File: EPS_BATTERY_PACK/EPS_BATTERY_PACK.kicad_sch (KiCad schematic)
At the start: 47 parts, among them J6001 PT_1000, J6002 HEATER, J6003 HEATER, J6004 Battery, Q6001 NVTFWS4D9N04XMTAG, Q6002 NVTFWS4D9N04XMTAG, U6001 BQ76920PW

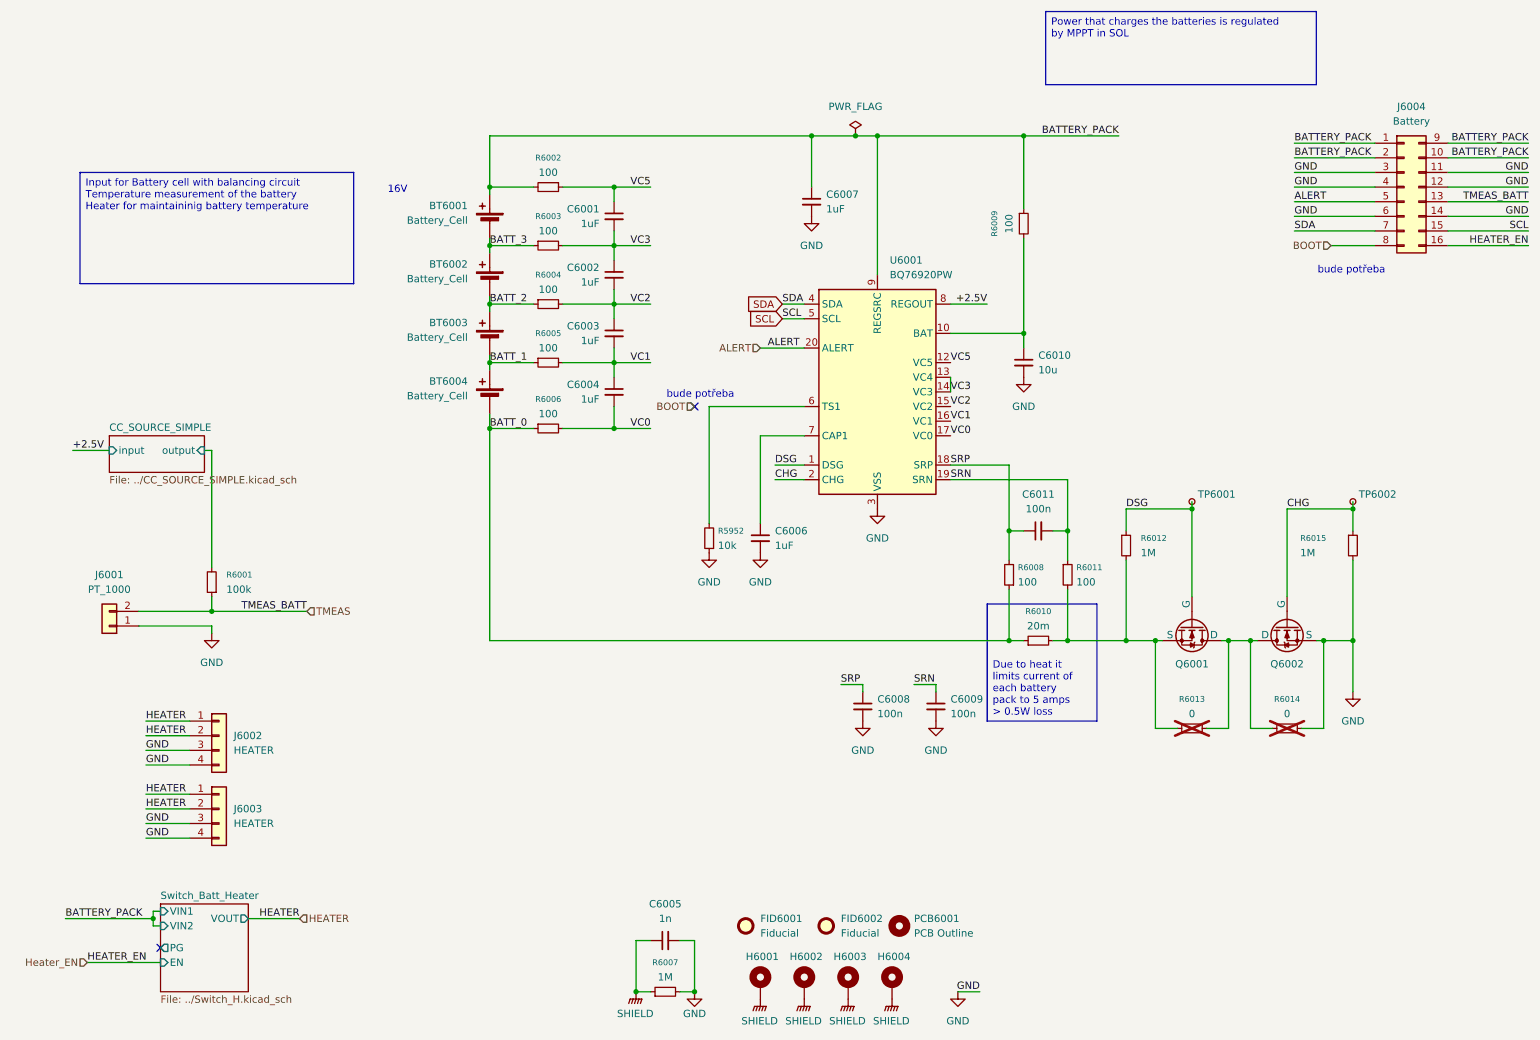
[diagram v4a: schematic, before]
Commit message: pcb progres for all components
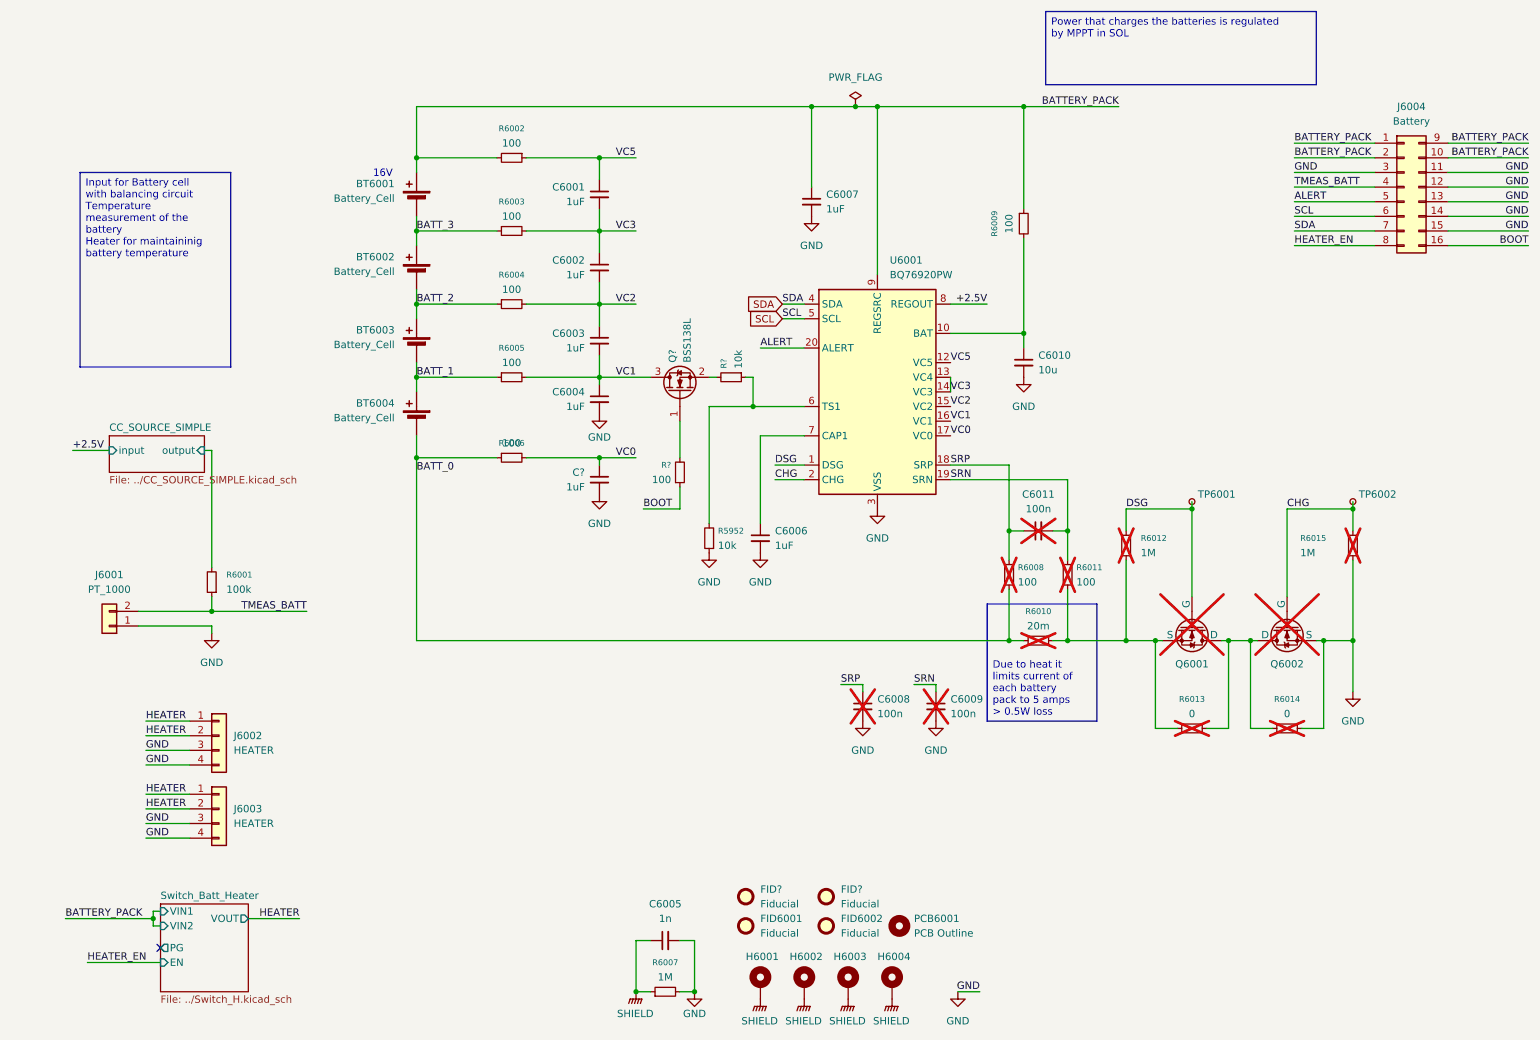
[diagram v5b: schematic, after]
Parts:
- added C?: 1uF, Capacitor_SMD:C_0603_1608Metric_Pad1.08x0.95mm_HandSolder, symbol Device:C_Small
- added FID? (x2): Fiducial, Fiducial:Fiducial_1mm_Mask2mm, symbol Mechanical:Fiducial
- added Q?: BSS138L, Package_TO_SOT_SMD:SOT-23, symbol VZLU_Transistor_FET:IRLML2803TRPBF
- added R?: 10k, Resistor_SMD:R_0603_1608Metric_Pad0.98x0.95mm_HandSolder, symbol Device:R_Small
- added R?: 100, Resistor_SMD:R_0603_1608Metric_Pad0.98x0.95mm_HandSolder, symbol Device:R_Small
- BT6001, BT6002, BT6003, BT6004: footprint Connector_PinSocket_2.54mm:PinSocket_1x02_P2.54mm_Vertical -> Outlines:BHC186501P-li-ion
- C6008, C6009, C6011, Q6001, Q6002, R6008, R6010, R6011, R6012, R6015: now not fitted
- J6002, J6003: footprint Connector_Molex:Molex_CLIK-Mate_502494-0470_1x04-1MP_P2.00mm_Horizontal -> Connector_PinHeader_2.54mm:PinHeader_1x04_P2.54mm_Vertical
- J6004: footprint Connector_Harwin:Harwin_Gecko-G125-FVX1605L0X_2x08_P1.25mm_Vertical -> Outlines:G125-MH11605L1P
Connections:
- net Heater_EN is gone; now on net BOOT: J6004.16 (Pin_16)
- net BOOT: now also R?.1; no longer J6004.8 (Pin_8)
- net GND: now also C6004.2, J6004.13 (Pin_13), J6004.15 (Pin_15), C?.2; no longer J6004.4 (Pin_4), J6004.6 (Pin_6)
- net SCL: now also J6004.6 (Pin_6); no longer J6004.15 (Pin_15)
- net VC0: now also C?.1; no longer C6004.2
- net VC1: now also Q?.3 (D)
- net at R5952.2, U6001.6 (TS1): now also R?.1
- net TMEAS renamed TMEAS_BATT
- net TMEAS_BATT: now also J6004.4 (Pin_4); no longer J6004.13 (Pin_13)
- new net: Q?.1 (G), R?.2
- new net: Q?.2 (S), R?.2
- new net HEATER_EN: J6004.8 (Pin_8)
- no-connect marks 2 -> 1
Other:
- note removed: "bude potřeba"
- moved on the sheet: BT6001, BT6002, BT6003, BT6004, C6001, C6002, C6003, C6004, R6002, R6003, R6004, R6005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
